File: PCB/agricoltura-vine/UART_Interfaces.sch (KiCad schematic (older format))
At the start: 7 parts, among them T4 BM04B-SRSS-TB(LF)(SN), T5 BM04B-SRSS-TB(LF)(SN), T6 BM04B-SRSS-TB(LF)(SN), T7 BM04B-SRSS-TB(LF)(SN), U2 74HC4052D

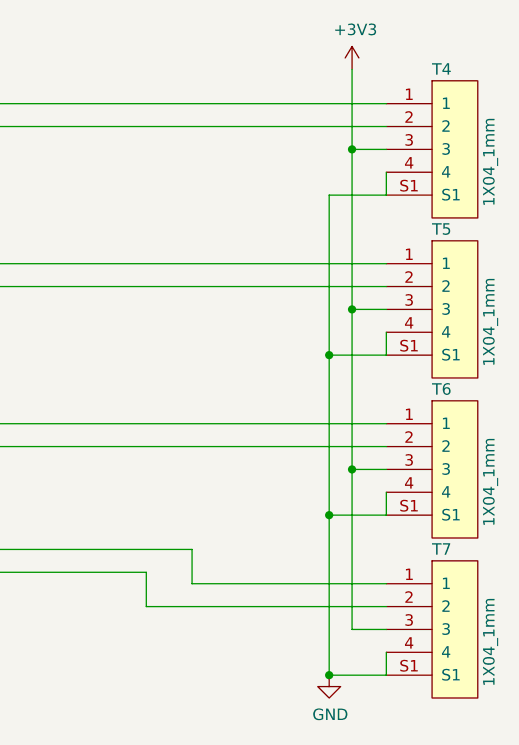
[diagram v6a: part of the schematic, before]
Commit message: Majopr Progress
Board shape enlarged to simplify layout and accomodate larger size parts for sisterboard like Ivy. QWIIC connectors flipped to be correct, signals were oriented incorrectly in past revisions.
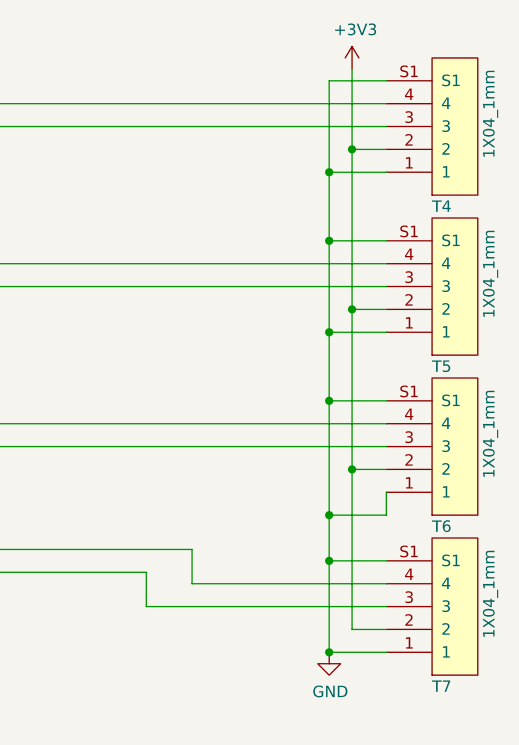
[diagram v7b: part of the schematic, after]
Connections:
- net +3V3: now also T4.2, T5.2, T6.2, T7.2; no longer T4.3, T5.3, T6.3, T7.3
- net GND: now also T4.1, T5.1, T6.1, T7.1; no longer T4.4, T5.4, T6.4, T7.4
- net UARTS1_RX: now also T4.4; no longer T4.1
- net UARTS1_TX: now also T4.3; no longer T4.2
- net UARTS2_RX: now also T5.4; no longer T5.1
- net UARTS2_TX: now also T5.3; no longer T5.2
- net UARTS3_RX: now also T6.4; no longer T6.1
- net UARTS3_TX: now also T6.3; no longer T6.2
- net UARTS4_RX: now also T7.4; no longer T7.1
- net UARTS4_TX: now also T7.3; no longer T7.2
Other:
- moved on the sheet: T4, T5, T6, T7

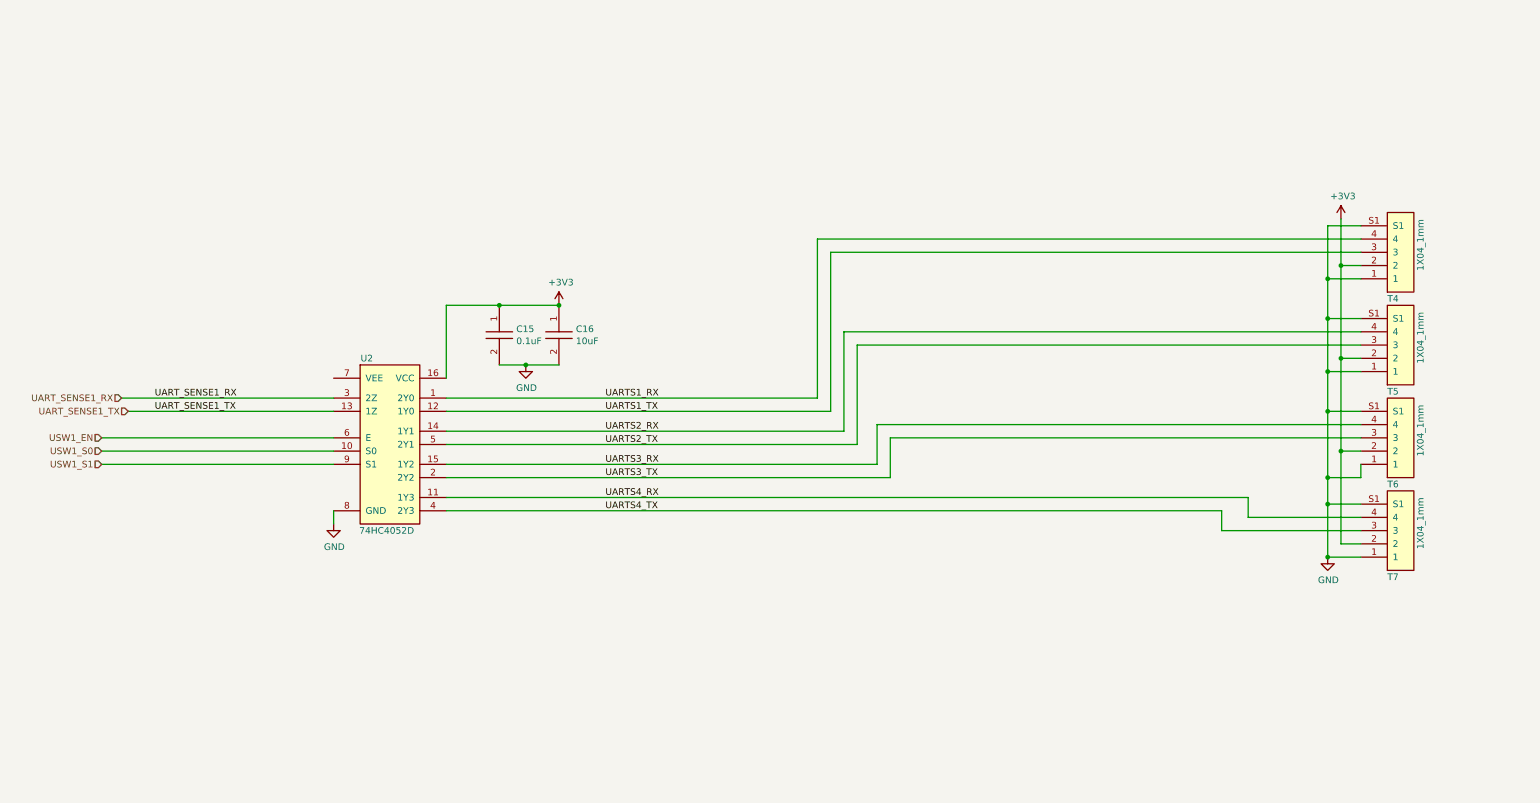
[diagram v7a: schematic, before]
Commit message: Relay Driver Circuit, Board Size Change
Added the Relay driver circuitry, increased size of board tobetter acccomodate relays, figuredout the powerplane topology to get 5Vs where it needs to go.
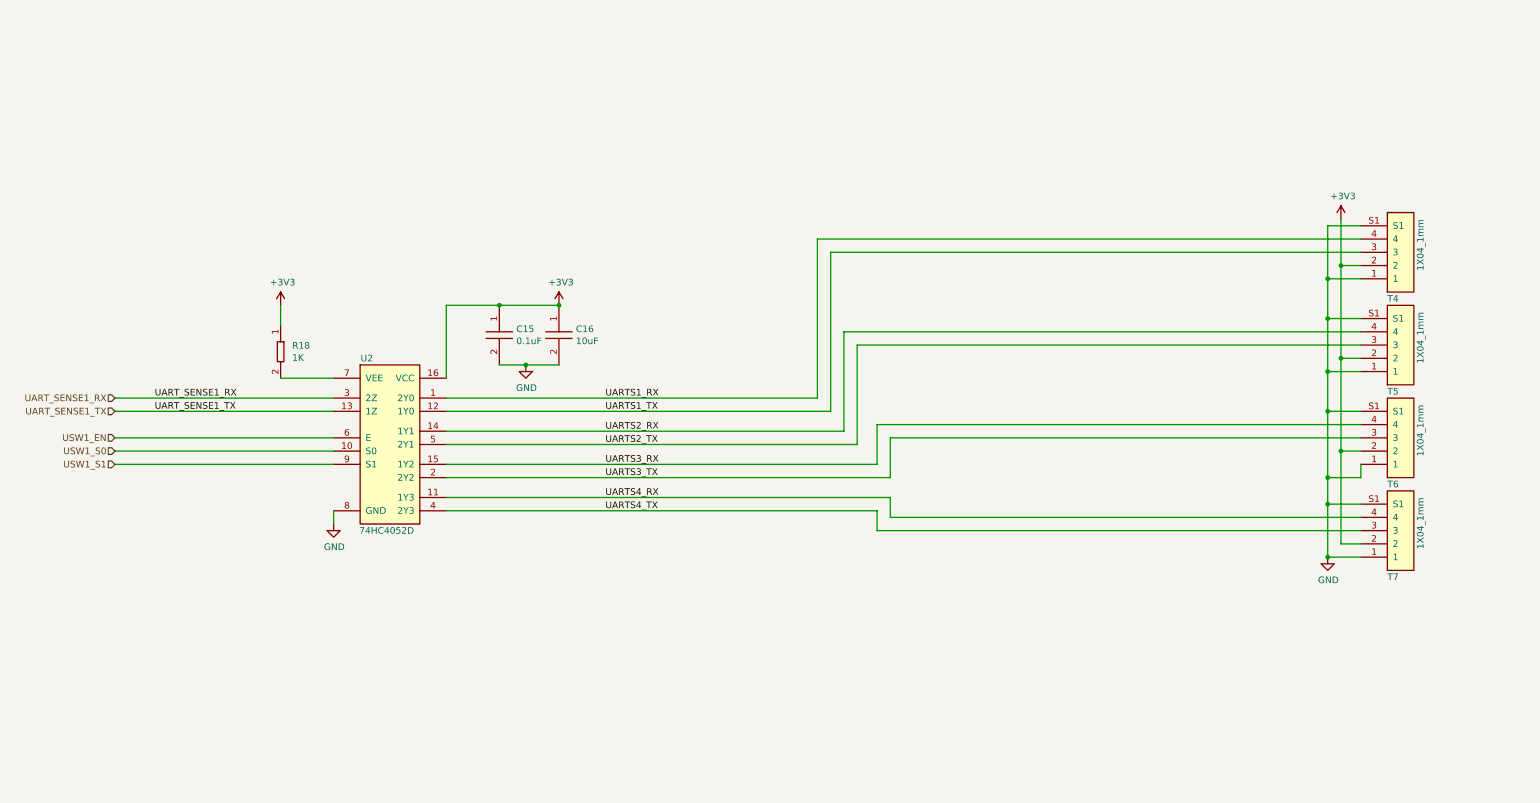
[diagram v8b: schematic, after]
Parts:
- added R18: RC0402FR-071KL, AVR-KiCAD-Lib-Resistors:R0402, symbol AVR-KiCAD-Lib-Resistors:RC0402FR-071KL
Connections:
- net +3V3: now also R18.1
- net at U2.7 (VEE): now also R18.2
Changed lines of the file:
@@
 	2850 4350 2850 4450
 Wire Wire Line
-	2850 3600 1300 3600
-Wire Wire Line
-	2850 3500 1250 3500
+	2850 3600 1200 3600
+Wire Wire Line
+	2850 3500 1200 3500
 Text Label 1500 3600 0    50   ~ 0
 UART_SENSE1_TX
 Text Label 1500 3500 0    50   ~ 0
 UART_SENSE1_RX
-Text HLabel 1300 3600 0    50   Input ~ 0
+Text HLabel 1200 3600 0    50   Input ~ 0
 UART_SENSE1_TX
-Text HLabel 1250 3500 0    50   Input ~ 0
+Text HLabel 1200 3500 0    50   Input ~ 0
 UART_SENSE1_RX
 $Comp
@@
 	1    0    0    -1
 $EndComp
-Text HLabel 1100 4000 0    50   Input ~ 0
+Text HLabel 1200 4000 0    50   Input ~ 0
 USW1_S1
-Text HLabel 1100 3900 0    50   Input ~ 0
+Text HLabel 1200 3900 0    50   Input ~ 0
 USW1_S0
-Text HLabel 1100 3800 0    50   Input ~ 0
+Text HLabel 1200 3800 0    50   Input ~ 0
 USW1_EN
 Wire Wire Line
-	2850 3800 1100 3800
-Wire Wire Line
-	1100 3900 2850 3900
-Wire Wire Line
-	2850 4000 1100 4000
+	2850 3800 1200 3800
+Wire Wire Line
+	1200 3900 2850 3900
+Wire Wire Line
+	2850 4000 1200 4000
 Wire Wire Line
 	10350 4700 10600 4700
@@
 	7050 3800 10600 3800
 Wire Wire Line
-	9750 4250 9750 4400
-Wire Wire Line
-	9750 4400 10600 4400
-Wire Wire Line
-	3700 4250 9750 4250
-Wire Wire Line
-	10600 4500 9550 4500
-Wire Wire Line
-	9550 4500 9550 4350
-Wire Wire Line
-	3700 4350 9550 4350
+	7050 4250 7050 4400
+Wire Wire Line
+	7050 4400 10600 4400
+Wire Wire Line
+	3700 4250 7050 4250
+Wire Wire Line
+	10600 4500 6950 4500
+Wire Wire Line
+	6950 4500 6950 4350
+Wire Wire Line
+	3700 4350 6950 4350
 Wire Wire Line
 	3700 4100 7050 4100
@@
 	10350 2200 10350 2600
 Connection ~ 10350 2600
+$Comp
+L AVR-KiCAD-Lib-Resistors:RC0402FR-071KL R?
+U 1 1 5F080A60
+P 2450 3150
+AR Path="/5EE82896/5F080A60" Ref="R?"  Part="1"
+AR Path="/5EE82702/5F080A60" Ref="R18"  Part="1"
+F 0 "R18" V 2404 3237 50  0000 L CNN
+F 1 "RC0402FR-071KL" V 2450 3238 50  0001 L CNN
+F 2 "AVR-KiCAD-Lib-Resistors:R0402" H 2450 3150 50  0001 C CNN
+F 3 "https://www.yageo.com/upload/media/product/productsearch/datasheet/rchip/PYu-RC_Group_51_RoHS_L_10.pdf" H 2450 3150 50  0001 C CNN
+F 4 "0.10000" H 2550 3400 50  0001 C CNN "Cost QTY: 1"
+F 5 "0.00289" H 2650 3500 50  0001 C CNN "Cost QTY: 1000"
+F 6 "0.00251" H 2750 3600 50  0001 C CNN "Cost QTY: 2500"
+F 7 "0.00207" H 2850 3700 50  0001 C CNN "Cost QTY: 5000"
+F 8 "0.00163" H 2950 3800 50  0001 C CNN "Cost QTY: 10000"
+F 9 "Yageo" H 3050 3900 50  0001 C CNN "MFR"
+F 10 "RC0402FR-071KL" H 3150 4000 50  0001 C CNN "MFR#"
+F 11 "Digikey" H 3250 4100 50  0001 C CNN "Vendor"
+F 12 "311-1.00KLRTR-ND" H 3350 4200 50  0001 C CNN "Vendor #"
+F 13 "AVR" H 3450 4300 50  0001 C CNN "Designer"
+F 14 "0.4mm" H 3550 4400 50  0001 C CNN "Height"
+F 15 "12/11/2019" H 4650 5500 50  0001 C CNN "Date Created"
+F 16 "12/11/2019" H 3650 4500 50  0001 C CNN "Date Modified"
+F 17 "Yes" H 3750 4600 50  0001 C CNN "Lead-Free ?"
+F 18 "1" H 3850 4700 50  0001 C CNN "RoHS Levels"
+F 19 "SMT" H 3950 4800 50  0001 C CNN "Mounting"
+F 20 "2" H 4050 4900 50  0001 C CNN "Pin Count #"
+F 21 "Active" H 4150 5000 50  0001 C CNN "Status"
+F 22 "1%" H 4250 5100 50  0001 C CNN "Tolerance"
+F 23 "Thick Film Resistor" H 4350 5200 50  0001 C CNN "Type"
+F 24 "*" H 4450 5300 50  0001 C CNN "Voltage"
+F 25 "0402" H 4550 5450 50  0001 C CNN "Package"
+F 26 "1K" V 2495 3237 50  0000 L CNN "_Value_"
+F 27 "*" H 4850 5750 50  0001 C CNN "Management_ID"
+F 28 " kOhms ±1% 0.063W, 1/16W Chip Resistor 0402 (1005 Metric) Moisture Resistant Thick Film" H 4850 5750 50  0001 C CNN "Description"
+	1    2450 3150
+	0    1    1    0
+$EndComp
+$Comp
+L power:+3V3 #PWR?
+U 1 1 5F084046
+P 2450 2800
+AR Path="/5EE82896/5F084046" Ref="#PWR?"  Part="1"
+AR Path="/5EE82702/5F084046" Ref="#PWR0112"  Part="1"
+F 0 "#PWR0112" H 2450 2650 50  0001 C CNN
+F 1 "+3V3" H 2465 2973 50  0000 C CNN
+F 2 "" H 2450 2800 50  0001 C CNN
+F 3 "" H 2450 2800 50  0001 C CNN
+	1    2450 2800
+	1    0    0    -1
+$EndComp
+Wire Wire Line
+	2450 2800 2450 2950
+Wire Wire Line
+	2450 3350 2850 3350
 $EndSCHEMATC
